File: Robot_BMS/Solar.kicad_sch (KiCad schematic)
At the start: 20 parts, among them J4 691137710002, U2 LM3488MM, U3 CSD18563Q5A

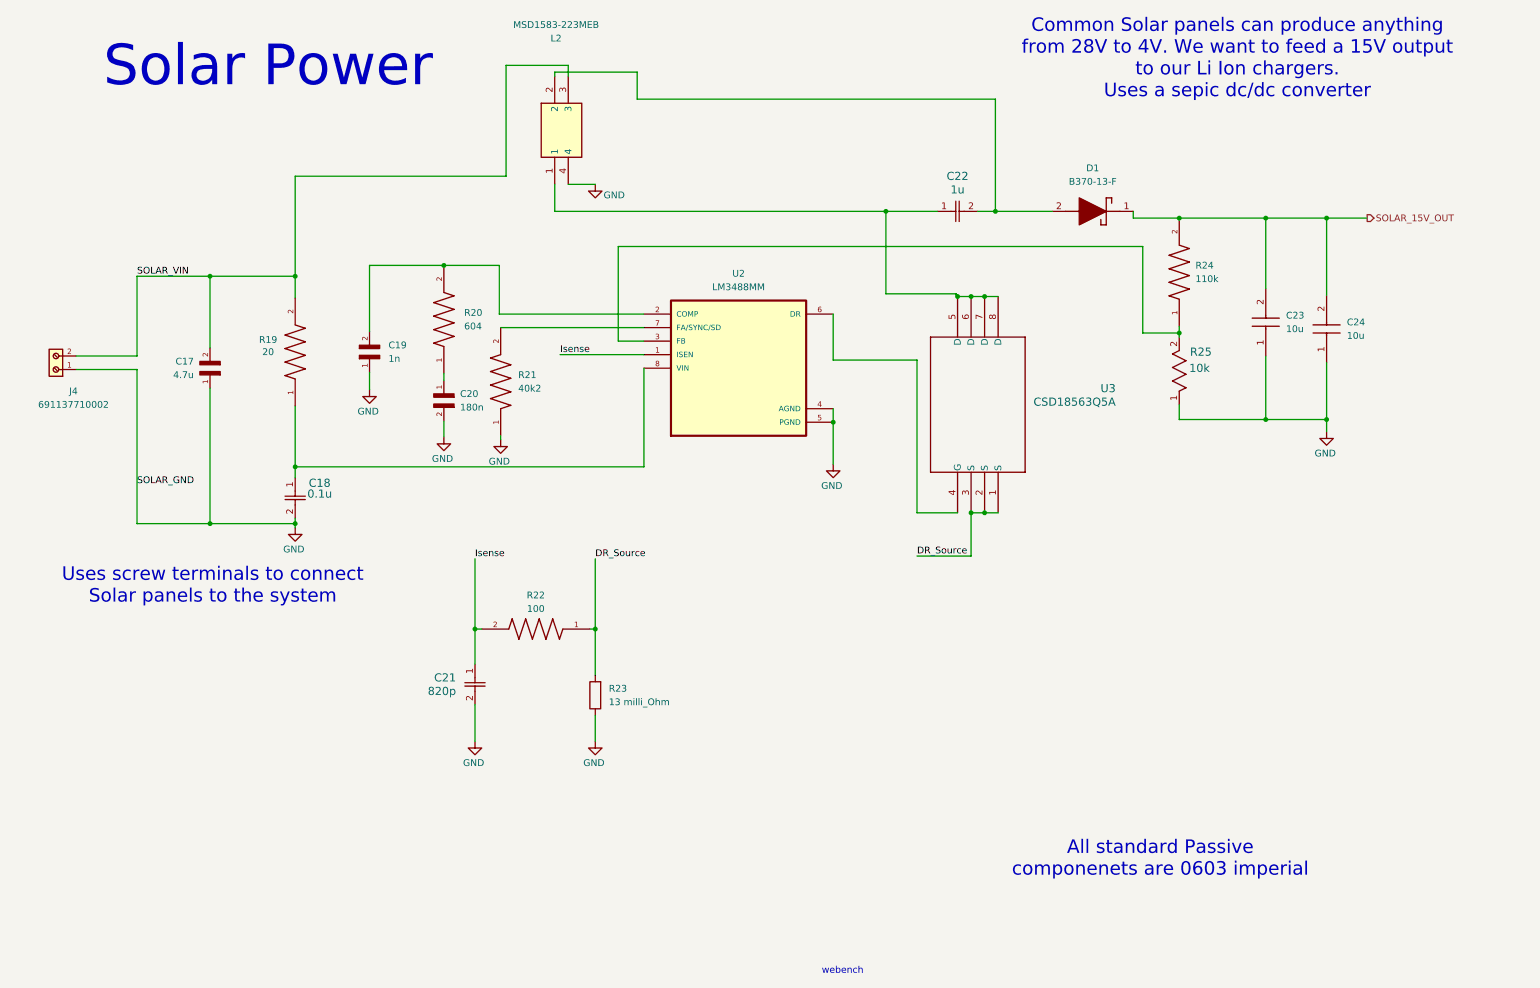
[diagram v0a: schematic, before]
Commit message: BOM done, with total price £40
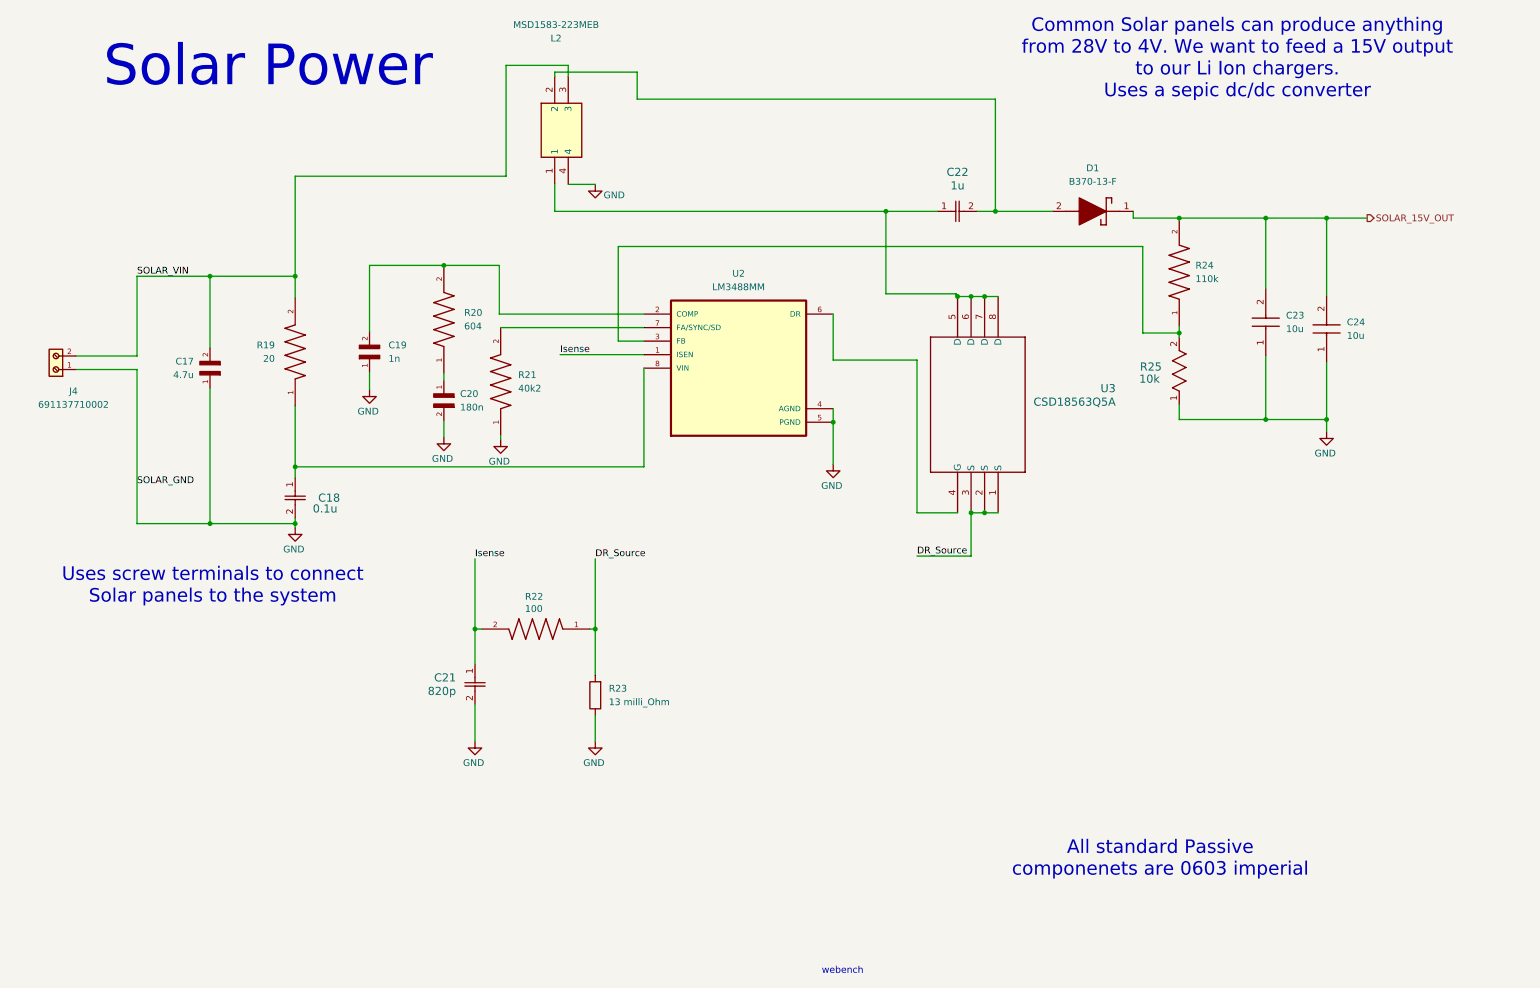
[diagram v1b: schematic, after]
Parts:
- C17: Manufacturer_Part_Number (none) -> ZRB18AR6YA475ME05L; Price None -> 0.198
- C18: Manufacturer_Part_Number (none) -> C0603C104K5RACAUTO; Price (none) -> 0.05
- C19: Manufacturer_Part_Number (none) -> SR201A102JARTR1; Price None -> 0.229
- C20: Manufacturer_Part_Number (none) -> CC0603KRX7R6BB184; Price None -> 0.103
- C21: Manufacturer_Part_Number (none) -> C0603X821K5RACAUTO; Price (none) -> 0.336
- C22: Manufacturer_Part_Number (none) -> C1608X5R1H105K080AB; Price (none) -> 0.156
- C23, C24: Price (none) -> 0.11
- D1: Price (none) -> 0.536
- J4: Manufacturer_Part_Number (none) -> 691137710002; Price (none) -> 0.336
- L2: Price (none) -> 3.84
- R19: Manufacturer_Part_Number (none) -> ERJPA3F20R0V; Price None -> 0.0512
- R20: Manufacturer_Part_Number (none) -> CRCW0603604RFKEA; Price None -> 0.079
- R21: Manufacturer_Part_Number (none) -> CRCW060340K2FKEAHP; Price None -> 0.0468
- R22: Manufacturer_Part_Number (none) -> AT0603DRE07100RL; Price None -> 0.068
- R23: Manufacturer_Part_Number (none) -> WFCP0603R0120FE66; Price (none) -> 0.48
- R24: Manufacturer_Part_Number (none) -> CRCW0603110KFKEAC; Price None -> 0.08
- R25: Manufacturer_Part_Number (none) -> RC0603FR-0710KL; Price (none) -> 0.096
- U2: Manufacturer_Part_Number (none) -> LM3488MM; Price (none) -> 2.13
- U3: Manufacturer_Part_Number (none) -> CSD18563Q5A; Price (none) -> 1.22

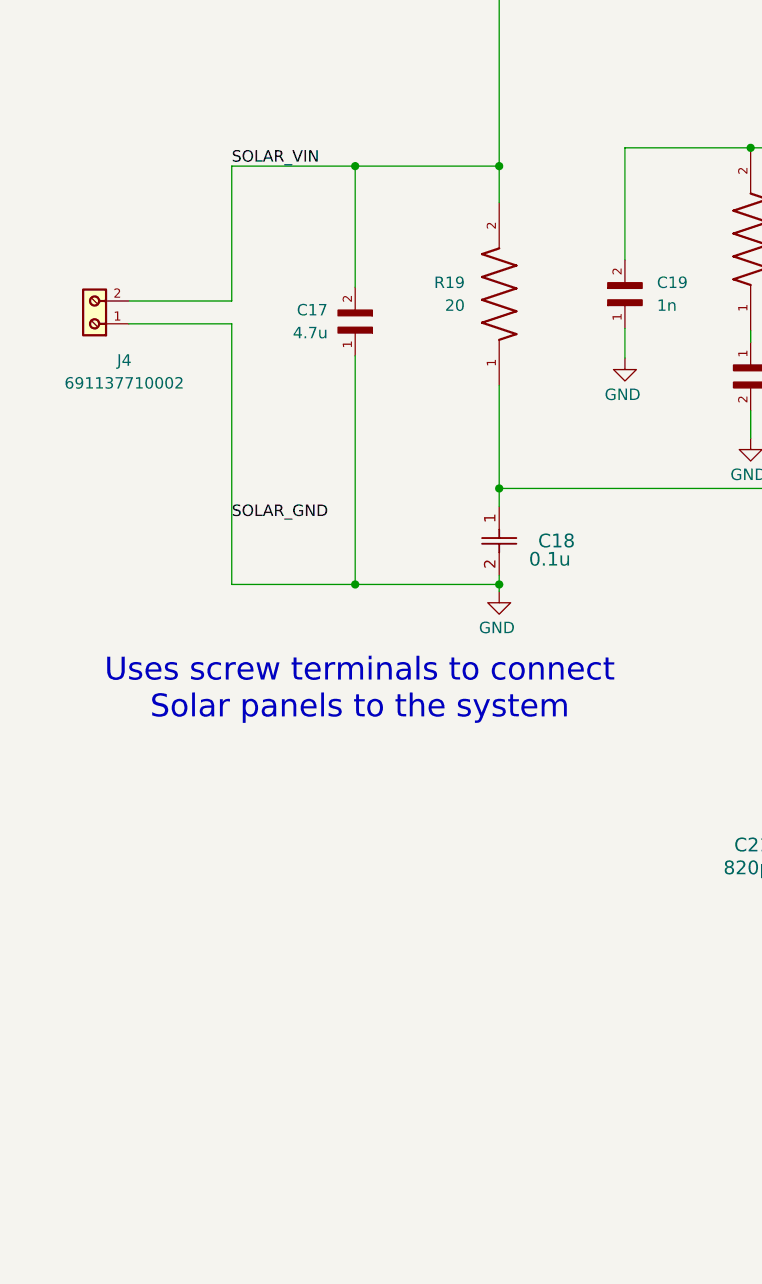
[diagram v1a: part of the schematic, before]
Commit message: switching usb c pd chip to ap33772 due to better support online
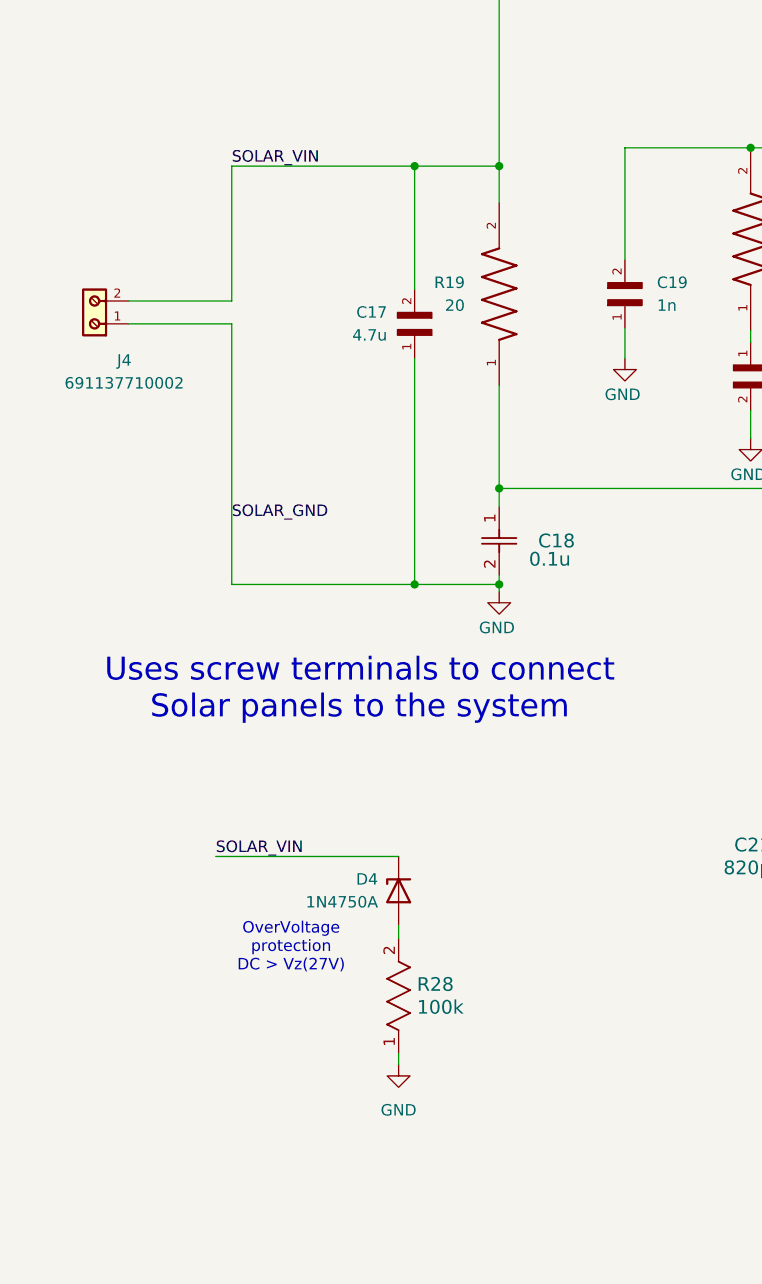
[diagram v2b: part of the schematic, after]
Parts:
- added D4: 1N4750A, Diode_THT:D_DO-41_SOD81_P10.16mm_Horizontal, symbol Diode:1N47xxA
- added R28: 100k, RobotBMS:RES_R0603_ROM, symbol ESR03EZPF1003:ESR03EZPF1003
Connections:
- net GND: now also R28.1
- net SOLAR_VIN: now also D4.1 (K)
- new net: D4.2 (A), R28.2
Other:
- note added: "OverVoltage protection DC > Vz(27V)"
- moved on the sheet: C17
